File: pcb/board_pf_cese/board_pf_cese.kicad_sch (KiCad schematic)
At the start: 14 parts, among them J1 Screw_Terminal_01x02, J10 Screw_Terminal_01x02, J2 Conn_01x04, J3 Conn_01x04, J4 Conn_01x04, J5 Conn_01x04, J6 Conn_01x15, J7 Conn_01x15, J8 Conn_01x08, J9 Conn_01x08

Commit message: actualizacion esquematico
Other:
- note added: "CONECTOR BATERIA 12V"
- note added: "CONECTOR BATERIA 3.7V"
- note removed: "CONECTOR BATERIA"
- moved on the sheet: J10
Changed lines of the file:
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@@
   (junction (at 160.02 83.82) (diameter 0) (color 0 0 0 0)
   )
-  (junction (at 125.73 165.1) (diameter 0) (color 0 0 0 0)
+  (junction (at 137.16 163.83) (diameter 0) (color 0 0 0 0)
   )
   (junction (at 49.53 52.07) (diameter 0) (color 0 0 0 0)
@@
     (stroke (width 0) (type default))
   )
-  (wire (pts (xy 226.06 142.24) (xy 163.83 142.24))
+  (wire (pts (xy 212.09 121.92) (xy 163.83 121.92))
     (stroke (width 0) (type default))
   )
@@
     (stroke (width 0) (type default))
   )
-  (wire (pts (xy 163.83 73.66) (xy 163.83 142.24))
+  (wire (pts (xy 163.83 73.66) (xy 163.83 121.92))
     (stroke (width 0) (type default))
   )
@@
     (stroke (width 0) (type default))
   )
-  (wire (pts (xy 134.62 165.1) (xy 125.73 165.1))
+  (wire (pts (xy 146.05 163.83) (xy 137.16 163.83))
     (stroke (width 0) (type default))
   )
@@
     (stroke (width 0) (type default))
   )
-  (wire (pts (xy 114.3 167.64) (xy 116.84 167.64))
-    (stroke (width 0) (type default))
-  )
-  (wire (pts (xy 226.06 138.43) (xy 226.06 142.24))
+  (wire (pts (xy 125.73 166.37) (xy 128.27 166.37))
+    (stroke (width 0) (type default))
+  )
+  (wire (pts (xy 212.09 138.43) (xy 212.09 121.92))
     (stroke (width 0) (type default))
   )
@@
     (stroke (width 0) (type default))
   )
-  (wire (pts (xy 153.67 73.66) (xy 163.83 73.66))
+  (wire (pts (xy 163.83 73.66) (xy 153.67 73.66))
     (stroke (width 0) (type default))
   )
@@
     (stroke (width 0) (type default))
   )
-  (wire (pts (xy 116.84 167.64) (xy 116.84 168.91))
+  (wire (pts (xy 128.27 166.37) (xy 128.27 167.64))
     (stroke (width 0) (type default))
   )
@@
     (stroke (width 0) (type default))
   )
-  (wire (pts (xy 134.62 162.56) (xy 134.62 165.1))
+  (wire (pts (xy 146.05 161.29) (xy 146.05 163.83))
     (stroke (width 0) (type default))
   )
@@
     (stroke (width 0) (type default))
   )
+  (polyline (pts (xy 85.09 130.81) (xy 190.5 130.81))
+    (stroke (width 0) (type default))
+  )
   (wire (pts (xy 228.6 90.17) (xy 223.52 90.17))
     (stroke (width 0) (type default))
@@
     (stroke (width 0) (type default))
   )
-  (wire (pts (xy 114.3 165.1) (xy 125.73 165.1))
+  (wire (pts (xy 125.73 163.83) (xy 137.16 163.83))
     (stroke (width 0) (type default))
   )
@@
     (stroke (width 0) (type default))
   )
-  (wire (pts (xy 125.73 165.1) (xy 125.73 161.29))
+  (wire (pts (xy 137.16 163.83) (xy 137.16 160.02))
     (stroke (width 0) (type default))
   )
@@
     (stroke (width 0) (type default))
   )
-  (wire (pts (xy 228.6 138.43) (xy 226.06 138.43))
+  (wire (pts (xy 212.09 138.43) (xy 228.6 138.43))
     (stroke (width 0) (type default))
   )
@@
     (effects (font (size 1.27 1.27) (thickness 0.254) bold) (justify right bottom))
   )
+  (text "CONECTOR BATERIA 12V" (at 116.84 142.24 0)
+    (effects (font (size 2.5 2.5) (thickness 0.6) bold) (justify left bottom))
+  )
   (text "sensor de\nluz UV\n\n" (at 260.35 139.7 0)
     (effects (font (size 1.27 1.27) (thickness 0.254) bold) (justify right bottom))
   )
-  (text "CONECTOR BATERIA " (at 26.67 26.67 0)
+  (text "CONECTOR BATERIA 3.7V" (at 26.67 26.67 0)
     (effects (font (size 2.5 2.5) (thickness 0.6) bold) (justify left bottom))
   )
@@
     )
   )
-  (symbol (lib_id "power:PWR_FLAG") (at 134.62 162.56 0) (unit 1)
-    (in_bom yes) (on_board yes) (dnp no)
-    (property "Reference" "#FLG03" (at 134.62 160.655 0)
-      (effects (font (size 1.27 1.27)) hide)
-    )
-    (property "Value" "PWR_FLAG" (at 134.62 158.75 0)
-      (effects (font (size 1.27 1.27)))
-    )
-    (property "Footprint" "" (at 134.62 162.56 0)
-      (effects (font (size 1.27 1.27)) hide)
-    )
-    (property "Datasheet" "~" (at 134.62 162.56 0)
+  (symbol (lib_id "power:PWR_FLAG") (at 146.05 161.29 0) (unit 1)
+    (in_bom yes) (on_board yes) (dnp no)
+    (property "Reference" "#FLG03" (at 146.05 159.385 0)
+      (effects (font (size 1.27 1.27)) hide)
+    )
+    (property "Value" "PWR_FLAG" (at 146.05 157.48 0)
+      (effects (font (size 1.27 1.27)))
+    )
+    (property "Footprint" "" (at 146.05 161.29 0)
+      (effects (font (size 1.27 1.27)) hide)
+    )
+    (property "Datasheet" "~" (at 146.05 161.29 0)
       (effects (font (size 1.27 1.27)) hide)
     )
@@
     )
   )
-  (symbol (lib_id "power:GND") (at 116.84 168.91 0) (unit 1)
-    (in_bom yes) (on_board yes) (dnp no) (fields_autoplaced)
-    (property "Reference" "#PWR022" (at 116.84 175.26 0)
-      (effects (font (size 1.27 1.27)) hide)
-    )
-    (property "Value" "GND" (at 116.84 173.99 0)
-      (effects (font (size 1.27 1.27)))
-    )
-    (property "Footprint" "" (at 116.84 168.91 0)
-      (effects (font (size 1.27 1.27)) hide)
-    )
-    (property "Datasheet" "" (at 116.84 168.91 0)
+  (symbol (lib_id "power:GND") (at 128.27 167.64 0) (unit 1)
+    (in_bom yes) (on_board yes) (dnp no) (fields_autoplaced)
+    (property "Reference" "#PWR022" (at 128.27 173.99 0)
+      (effects (font (size 1.27 1.27)) hide)
+    )
+    (property "Value" "GND" (at 128.27 172.72 0)
+      (effects (font (size 1.27 1.27)))
+    )
+    (property "Footprint" "" (at 128.27 167.64 0)
+      (effects (font (size 1.27 1.27)) hide)
+    )
+    (property "Datasheet" "" (at 128.27 167.64 0)
       (effects (font (size 1.27 1.27)) hide)
     )
@@
     )
   )
-  (symbol (lib_id "Connector:Screw_Terminal_01x02") (at 109.22 165.1 0) (mirror y) (unit 1)
-    (in_bom yes) (on_board yes) (dnp no) (fields_autoplaced)
-    (property "Reference" "J10" (at 109.22 158.75 0)
-      (effects (font (size 1.27 1.27)))
-    )
-    (property "Value" "Screw_Terminal_01x02" (at 109.22 161.29 0)
-      (effects (font (size 1.27 1.27)))
-    )
-    (property "Footprint" "TerminalBlock_Phoenix:TerminalBlock_Phoenix_MPT-0,5-2-2.54_1x02_P2.54mm_Horizontal" (at 109.22 165.1 0)
-      (effects (font (size 1.27 1.27)) hide)
-    )
-    (property "Datasheet" "~" (at 109.22 165.1 0)
+  (symbol (lib_id "Connector:Screw_Terminal_01x02") (at 120.65 163.83 0) (mirror y) (unit 1)
+    (in_bom yes) (on_board yes) (dnp no) (fields_autoplaced)
+    (property "Reference" "J10" (at 120.65 157.48 0)
+      (effects (font (size 1.27 1.27)))
+    )
+    (property "Value" "Screw_Terminal_01x02" (at 120.65 160.02 0)
+      (effects (font (size 1.27 1.27)))
+    )
+    (property "Footprint" "TerminalBlock_Phoenix:TerminalBlock_Phoenix_MPT-0,5-2-2.54_1x02_P2.54mm_Horizontal" (at 120.65 163.83 0)
+      (effects (font (size 1.27 1.27)) hide)
+    )
+    (property "Datasheet" "~" (at 120.65 163.83 0)
       (effects (font (size 1.27 1.27)) hide)
     )
@@
     )
   )
-  (symbol (lib_id "power:+12V") (at 125.73 161.29 0) (unit 1)
-    (in_bom yes) (on_board yes) (dnp no) (fields_autoplaced)
-    (property "Reference" "#PWR021" (at 125.73 165.1 0)
-      (effects (font (size 1.27 1.27)) hide)
-    )
-    (property "Value" "+12V" (at 125.73 156.21 0)
-      (effects (font (size 1.27 1.27)))
-    )
-    (property "Footprint" "" (at 125.73 161.29 0)
-      (effects (font (size 1.27 1.27)) hide)
-    )
-    (property "Datasheet" "" (at 125.73 161.29 0)
-      (effects (font (size 1.27 1.27)) hide)
-    )
+  (symbol (lib_id "power:+12V") (at 137.16 160.02 0) (unit 1)
+    (in_bom yes) (on_board yes) (dnp no) (fields_autoplaced)
+    (property "Reference" "#PWR021" (at 137.16 163.83 0)
+      (effects (font (size 1.27 1.27)) hide)
+    )
+    (property "Value" "+12V" (at 137.16 154.94 0)
+      (effects (font (size 1.27 1.27)))
+    )
+    (property "Footprint" "" (at 137.16 160.02 0)
+      (effects (font (size 1.27 1.27)) hide)
+    )
+    (property "Datasheet" "" (at 137.16 160.02 0)
+      (effects (font (size 1.27 1.27)) hide)
+    )

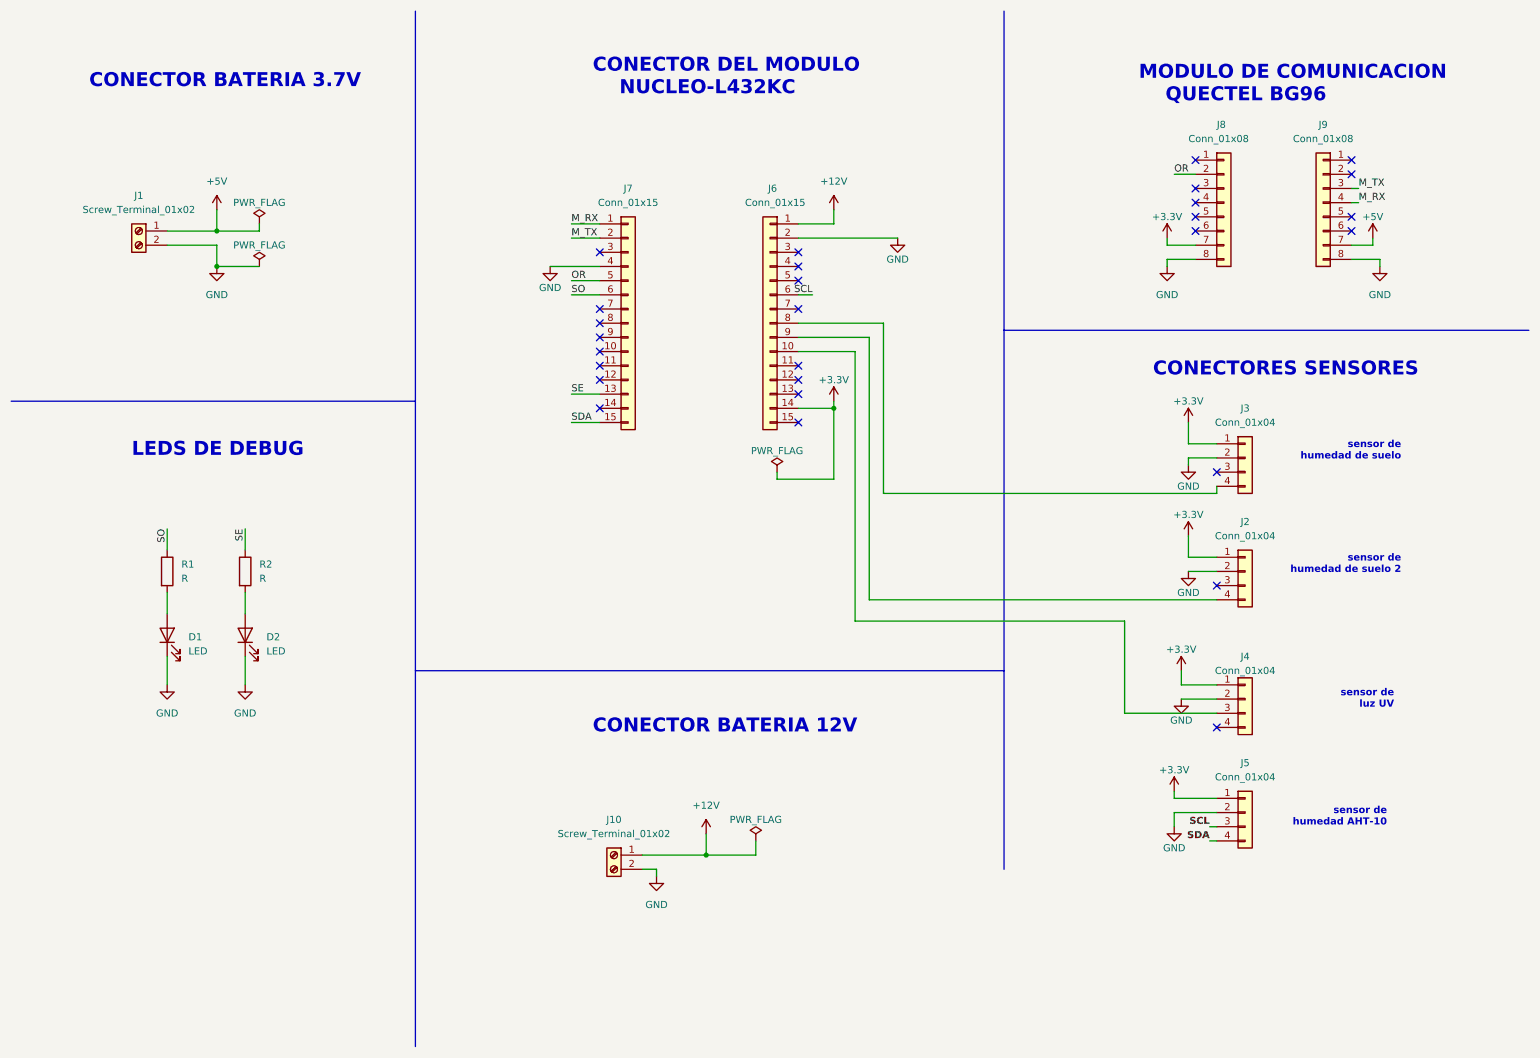
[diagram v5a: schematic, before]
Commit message: se adiciono conn uart2 para debug
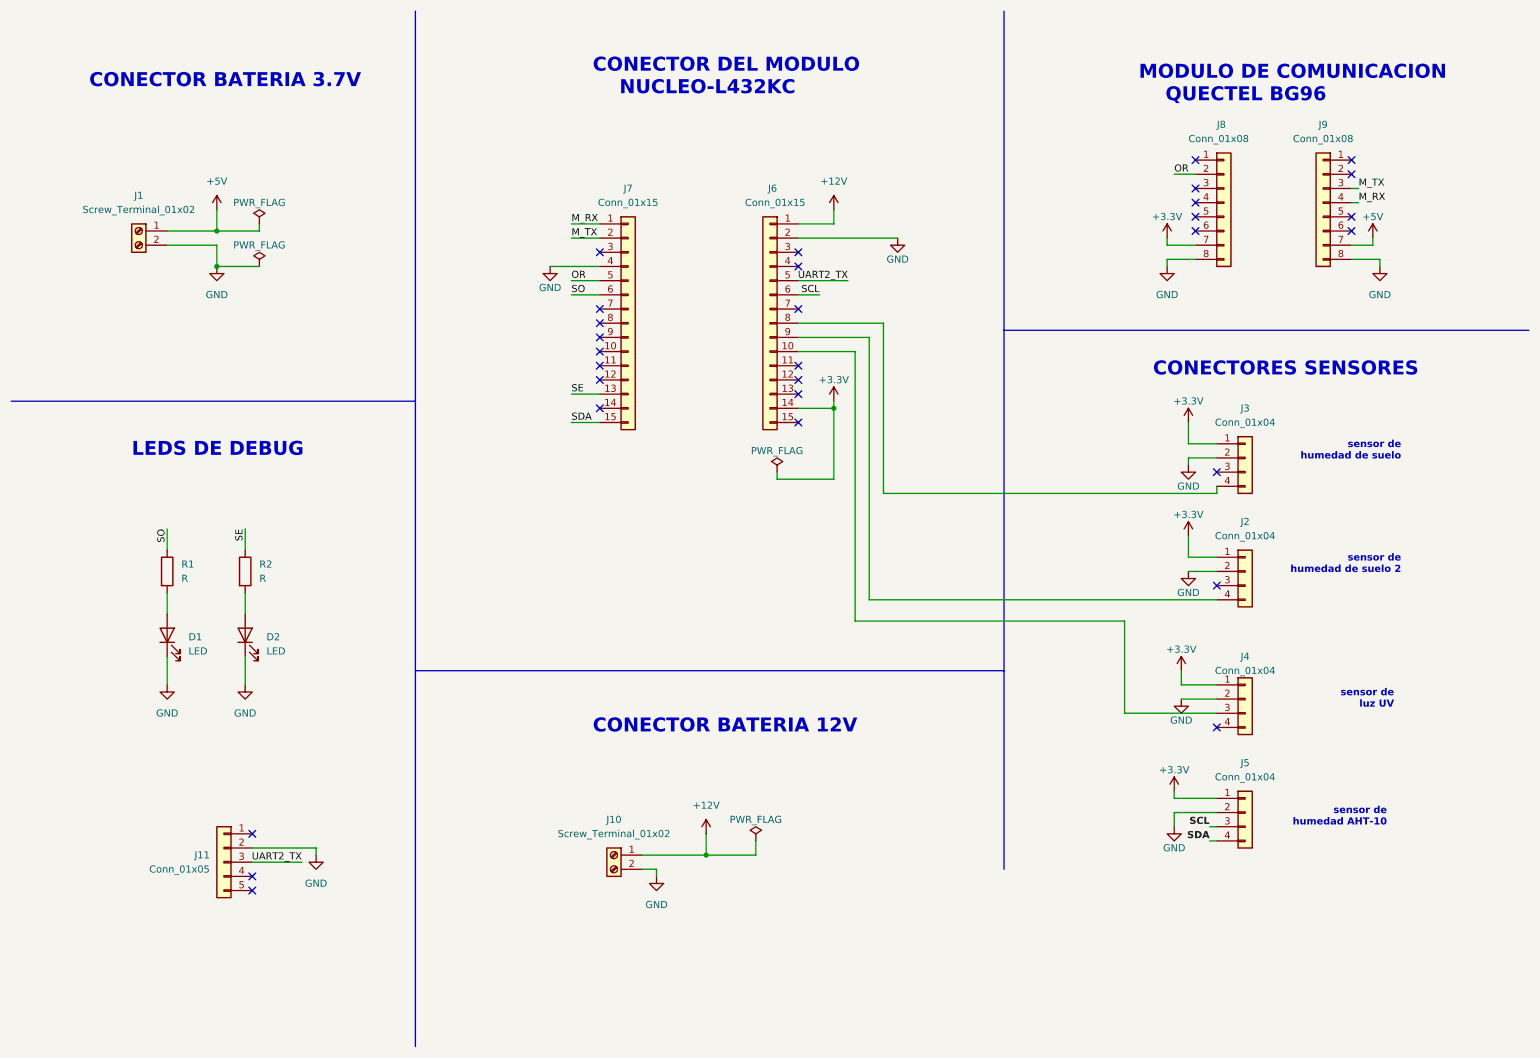
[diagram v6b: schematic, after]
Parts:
- added J11: Conn_01x05, Connector_PinSocket_2.54mm:PinSocket_1x05_P2.54mm_Vertical, symbol Connector_Generic:Conn_01x05
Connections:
- net GND: now also J11.2 (Pin_2)
- net UART2_TX: now reaches J6.5 (Pin_5)
- net UART2_TX: now also J11.3 (Pin_3)
- no-connect marks 28 -> 30
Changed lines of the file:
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@@
   (no_connect (at 153.67 76.2))
   (no_connect (at 252.73 41.91))
+  (no_connect (at 55.88 170.18))
   (no_connect (at 153.67 78.74))
   (no_connect (at 118.11 83.82))
   (no_connect (at 252.73 39.37))
   (no_connect (at 153.67 66.04))
+  (no_connect (at 55.88 167.64))
   (no_connect (at 153.67 81.28))
   (no_connect (at 118.11 76.2))
@@
   (no_connect (at 224.79 39.37))
   (no_connect (at 118.11 55.88))
+  (no_connect (at 55.88 160.02))
   (no_connect (at 153.67 58.42))
   (no_connect (at 224.79 52.07))
-  (no_connect (at 153.67 60.96))
   (no_connect (at 153.67 55.88))
   (no_connect (at 224.79 44.45))
@@
     (stroke (width 0) (type default))
   )
+  (wire (pts (xy 64.77 165.1) (xy 55.88 165.1))
+    (stroke (width 0) (type default))
+  )
   (wire (pts (xy 252.73 54.61) (xy 256.54 54.61))
     (stroke (width 0) (type default))
@@
     (stroke (width 0) (type default))
   )
-  (wire (pts (xy 156.21 63.5) (xy 153.67 63.5))
+  (wire (pts (xy 157.48 63.5) (xy 153.67 63.5))
     (stroke (width 0) (type default))
   )
@@
     (stroke (width 0) (type default))
   )
+  (wire (pts (xy 162.56 60.96) (xy 153.67 60.96))
+    (stroke (width 0) (type default))
+  )
+  (wire (pts (xy 67.31 162.56) (xy 67.31 163.83))
+    (stroke (width 0) (type default))
+  )
   (wire (pts (xy 40.64 116.84) (xy 40.64 120.65))
     (stroke (width 0) (type default))
@@
   )
   (wire (pts (xy 252.73 57.15) (xy 257.81 57.15))
+    (stroke (width 0) (type default))
+  )
+  (wire (pts (xy 55.88 162.56) (xy 67.31 162.56))
     (stroke (width 0) (type default))
   )
@@
     (effects (font (size 1.27 1.27)) (justify left bottom))
   )
+  (label "UART2_TX" (at 64.77 165.1 180) (fields_autoplaced)
+    (effects (font (size 1.27 1.27)) (justify right bottom))
+  )
   (label "M_TX" (at 113.03 53.34 0) (fields_autoplaced)
     (effects (font (size 1.27 1.27)) (justify left bottom))
@@
     (effects (font (size 1.27 1.27) bold) (justify right bottom))
   )
-  (label "SCL" (at 156.21 63.5 180) (fields_autoplaced)
+  (label "SCL" (at 157.48 63.5 180) (fields_autoplaced)
     (effects (font (size 1.27 1.27)) (justify right bottom))
   )
   (label "M_TX" (at 254 44.45 0) (fields_autoplaced)
     (effects (font (size 1.27 1.27)) (justify left bottom))
+  )
+  (label "UART2_TX" (at 162.56 60.96 180) (fields_autoplaced)
+    (effects (font (size 1.27 1.27)) (justify right bottom))
   )
   (label "SO" (at 40.64 105.41 270) (fields_autoplaced)
@@
         (path "/f972b6a0-1e3e-4ffa-a809-a80b99cd3c3e"
           (reference "#PWR017") (unit 1)
+        )
+      )
+    )
+  )
+  (symbol (lib_id "Connector_Generic:Conn_01x05") (at 50.8 165.1 0) (mirror y) (unit 1)
+    (in_bom yes) (on_board yes) (dnp no)
+    (property "Reference" "J11" (at 48.26 163.83 0)
+      (effects (font (size 1.27 1.27)) (justify left))
+    )
+    (property "Value" "Conn_01x05" (at 48.26 166.37 0)
+      (effects (font (size 1.27 1.27)) (justify left))
+    )
+    (property "Footprint" "Connector_PinSocket_2.54mm:PinSocket_1x05_P2.54mm_Vertical" (at 50.8 165.1 0)
+      (effects (font (size 1.27 1.27)) hide)
+    )
+    (property "Datasheet" "~" (at 50.8 165.1 0)
+      (effects (font (size 1.27 1.27)) hide)
+    )
+    (pin "1")
+    (pin "2")
+    (pin "3")
+    (pin "4")
+    (pin "5")
+    (instances
+      (project "board_pf_cese"
+        (path "/f972b6a0-1e3e-4ffa-a809-a80b99cd3c3e"
+          (reference "J11") (unit 1)
         )
       )
@@
         )
       )
+    )
+  )
+  (symbol (lib_id "power:GND") (at 67.31 163.83 0) (unit 1)
+    (in_bom yes) (on_board yes) (dnp no) (fields_autoplaced)
+    (property "Reference" "#PWR023" (at 67.31 170.18 0)
+      (effects (font (size 1.27 1.27)) hide)
+    )
+    (property "Value" "GND" (at 67.31 168.91 0)
+      (effects (font (size 1.27 1.27)))
+    )
+    (property "Footprint" "" (at 67.31 163.83 0)
+      (effects (font (size 1.27 1.27)) hide)
+    )
+    (property "Datasheet" "" (at 67.31 163.83 0)
+      (effects (font (size 1.27 1.27)) hide)
+    )
+    (pin "1")
+    (instances
+      (project "board_pf_cese"
+        (path "/f972b6a0-1e3e-4ffa-a809-a80b99cd3c3e"
+          (reference "#PWR023") (unit 1)
+        )
+      )

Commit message: update esquematico
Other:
- note added: "UART2 DEBUG"
- moved on the sheet: J10, J11

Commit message: finalizacion v1
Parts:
- D1, D2: footprint LED_THT:LED_D3.0mm -> LED_THT:LED_D5.0mm
- J1, J10: footprint TerminalBlock_Phoenix:TerminalBlock_Phoenix_MPT-0,5-2-2.54_1x02_P2.54mm_Horizontal -> TerminalBlock_Phoenix:TerminalBlock_Phoenix_MKDS-1,5-2_1x02_P5.00mm_Horizontal
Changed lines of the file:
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@@
       (effects (font (size 1.27 1.27)))
     )
-    (property "Footprint" "TerminalBlock_Phoenix:TerminalBlock_Phoenix_MPT-0,5-2-2.54_1x02_P2.54mm_Horizontal" (at 35.56 52.07 0)
+    (property "Footprint" "TerminalBlock_Phoenix:TerminalBlock_Phoenix_MKDS-1,5-2_1x02_P5.00mm_Horizontal" (at 35.56 52.07 0)
       (effects (font (size 1.27 1.27)) hide)
     )
@@
       (effects (font (size 1.27 1.27)))
     )
-    (property "Footprint" "TerminalBlock_Phoenix:TerminalBlock_Phoenix_MPT-0,5-2-2.54_1x02_P2.54mm_Horizontal" (at 129.54 165.1 0)
+    (property "Footprint" "TerminalBlock_Phoenix:TerminalBlock_Phoenix_MKDS-1,5-2_1x02_P5.00mm_Horizontal" (at 129.54 165.1 0)
       (effects (font (size 1.27 1.27)) hide)
     )
@@
       (effects (font (size 1.27 1.27)) (justify right))
     )
-    (property "Footprint" "LED_THT:LED_D3.0mm" (at 40.64 124.46 0)
+    (property "Footprint" "LED_THT:LED_D5.0mm" (at 40.64 124.46 0)
       (effects (font (size 1.27 1.27)) hide)
     )
@@
       (effects (font (size 1.27 1.27)) (justify right))
     )
-    (property "Footprint" "LED_THT:LED_D3.0mm" (at 54.61 124.46 0)
-      (effects (font (size 1.27 1.27)) hide)
-    )
+    (property "Footprint" "LED_THT:LED_D5.0mm" (at 54.61 124.46 0)
+      (effects (font (size 1.27 1.27)) hide)
+    )
